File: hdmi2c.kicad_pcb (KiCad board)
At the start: 2 copper layers, 42 x 24 mm, 16 parts, among them J7 HDMI1, SW2 B3U-1000P, SW3 B3U-1000P, U3 XIAO ESP32-C6, U4 TPD12S016PWR

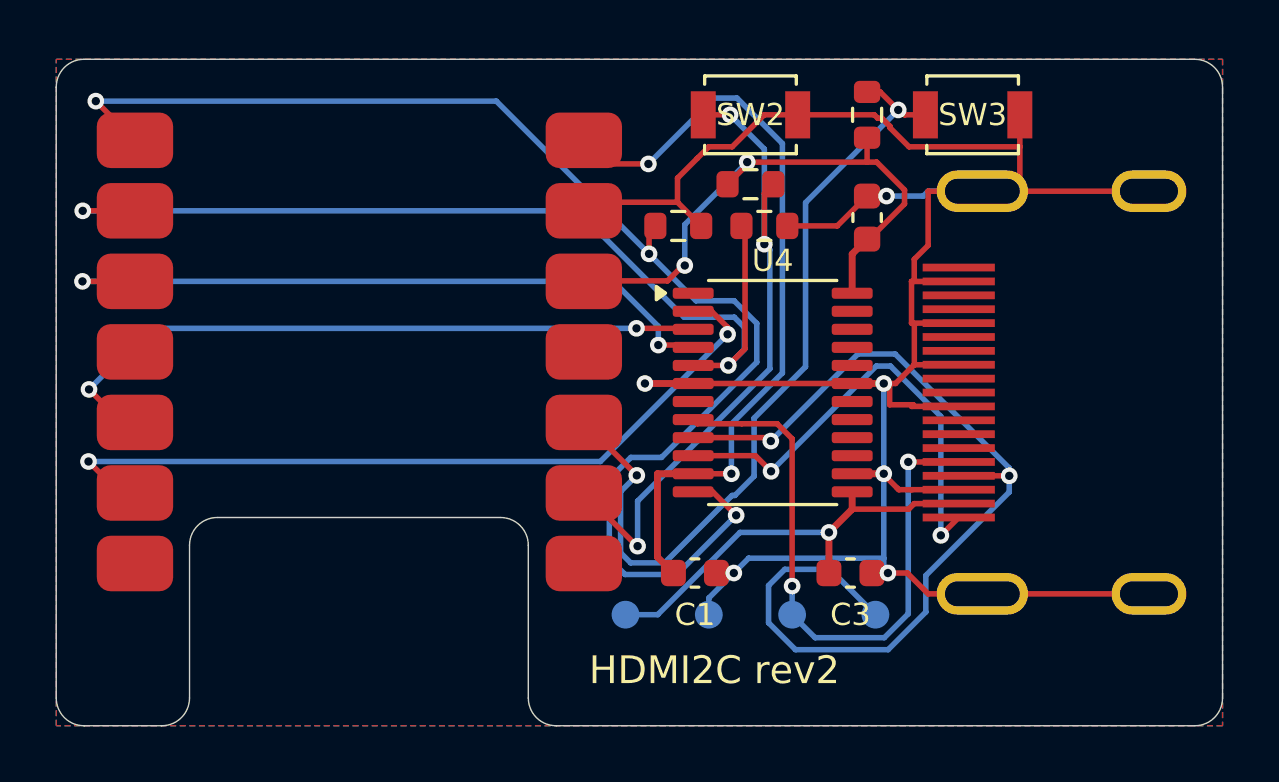
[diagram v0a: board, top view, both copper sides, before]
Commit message: Update creation dates and enhance BOM files for rev2 prototype
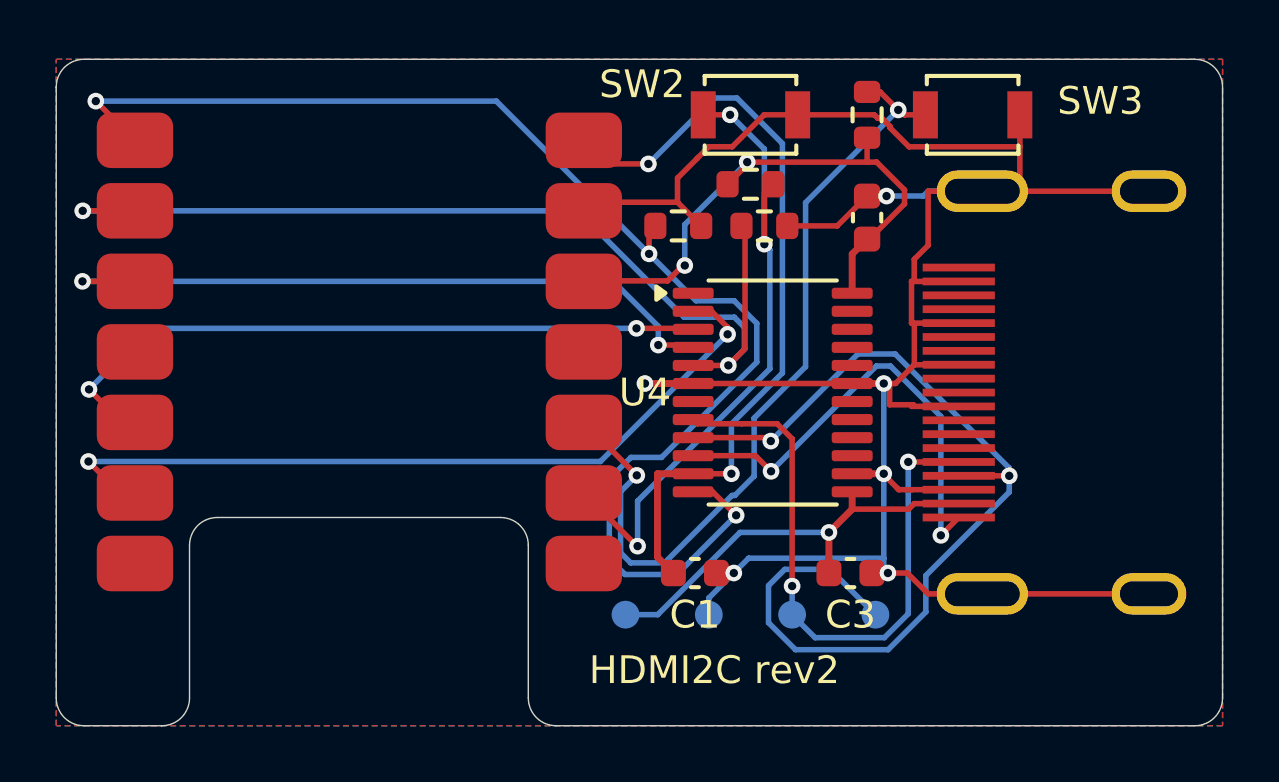
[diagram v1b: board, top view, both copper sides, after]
